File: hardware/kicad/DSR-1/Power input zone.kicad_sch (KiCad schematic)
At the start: 0 parts

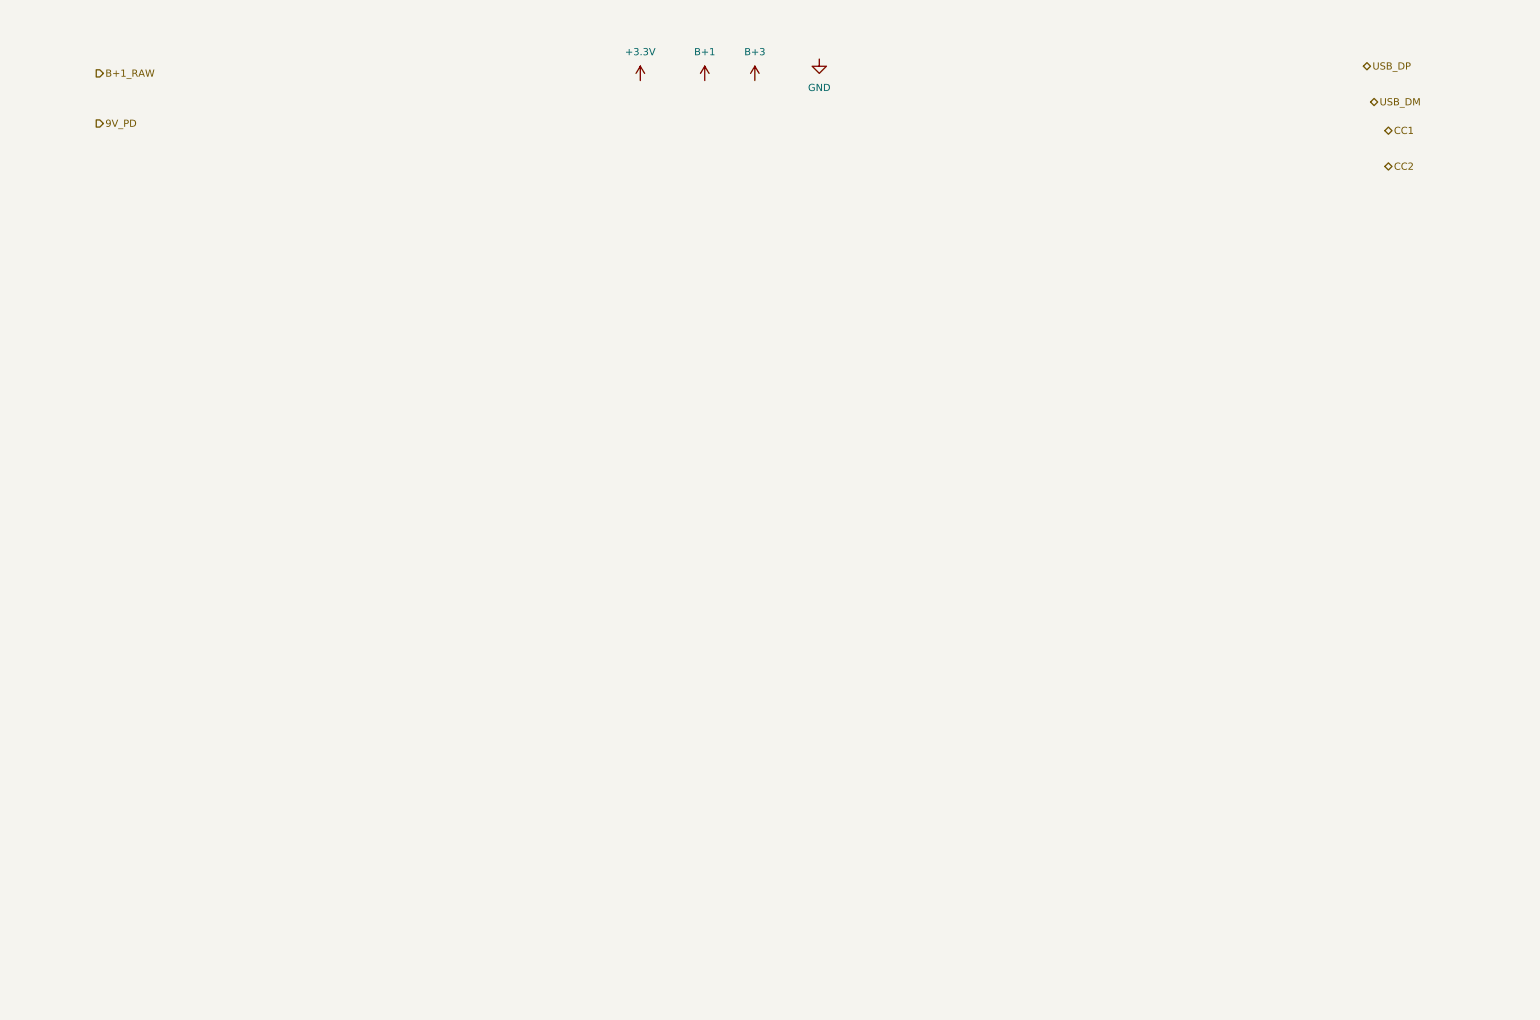
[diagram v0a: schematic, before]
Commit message: updated project symbol library ans started routing power input schematic
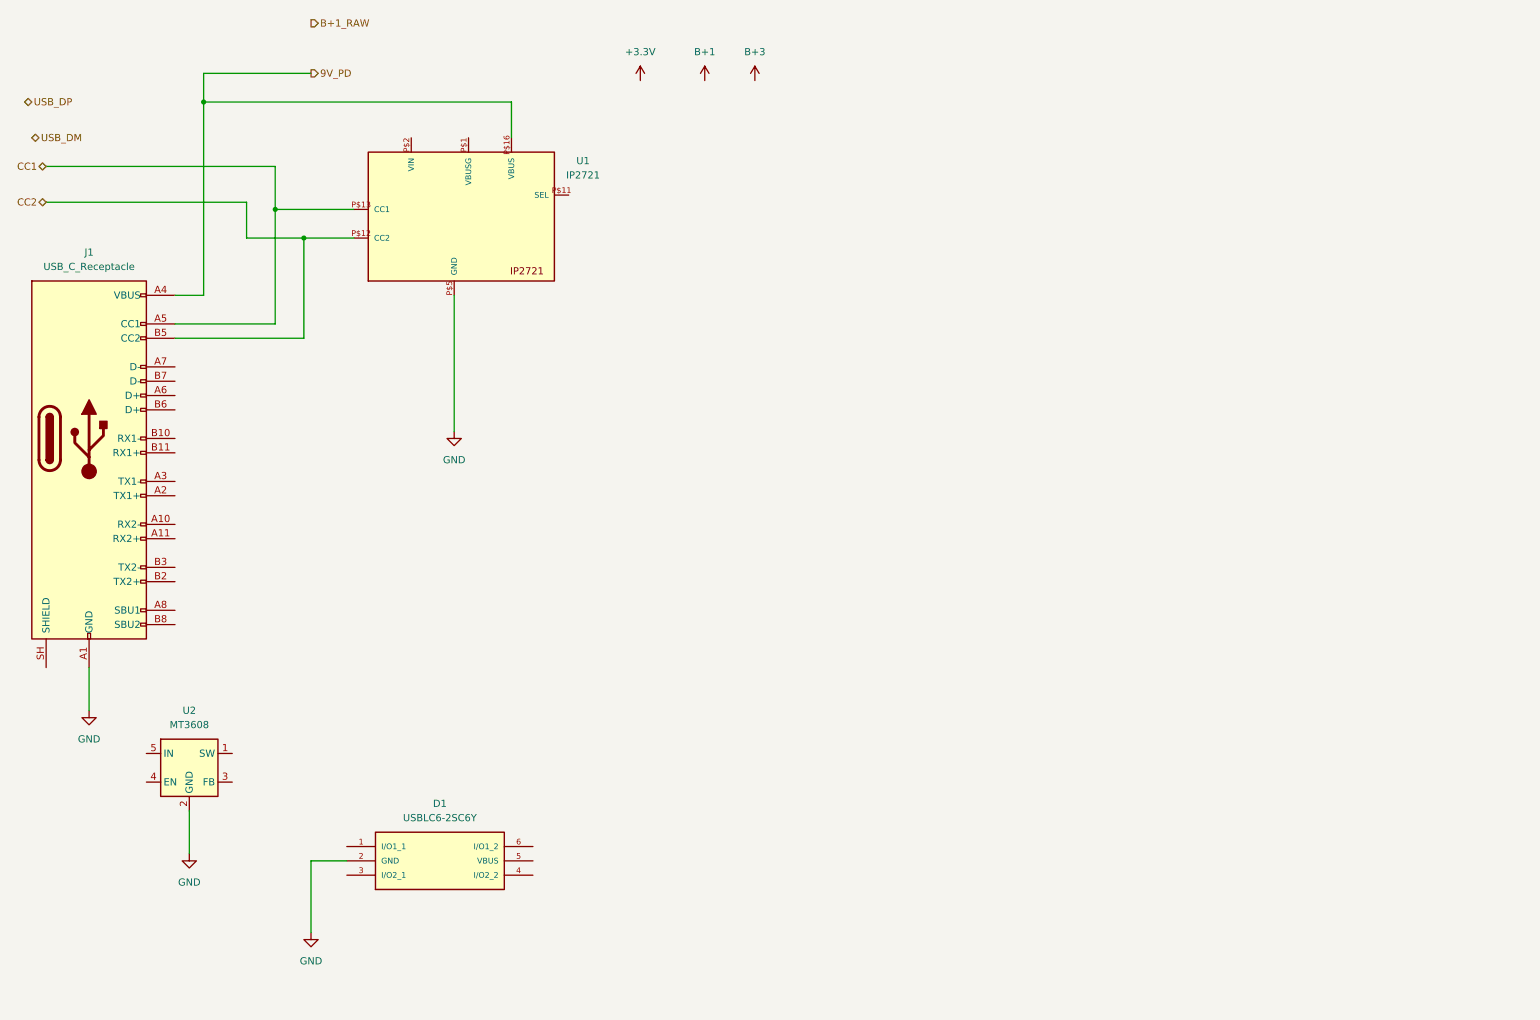
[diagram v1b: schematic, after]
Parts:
- added D1: USBLC6-2SC6Y, USBLC6-2SC6Y:SOT95P280X145-6N, symbol DSR-1:USBLC6-2SC6Y
- added J1: USB_C_Receptacle, symbol DSR-1:USB_C_Receptacle
- added U1: IP2721, IP2721:TSSOP16, symbol DSR-1:IP2721
- added U2: MT3608, Package_TO_SOT_SMD:SOT-23-6, symbol DSR-1:MT3608
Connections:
- net 9V_PD: now also J1.A4 (VBUS), J1.A9 (VBUS), J1.B4 (VBUS), J1.B9 (VBUS), U1.P$16 (VBUS)
- net CC1: now also J1.A5 (CC1), U1.P$13 (CC1)
- net CC2: now also J1.B5 (CC2), U1.P$12 (CC2)
- net GND: now also D1.2 (GND), J1.A1 (GND), J1.A12 (GND), J1.B1 (GND), J1.B12 (GND), U1.P$5 (GND), U2.2 (GND)

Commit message: Completed Power Input Sheet Variant A
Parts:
- removed U2: MT3608, Package_TO_SOT_SMD:SOT-23-6, symbol DSR-1:MT3608
- added C1: 4.7uf, symbol Device:C_US
- added C2: 10uf, symbol Device:C_US
- added C3: 100nf, symbol Device:C_US
- added C4: 22uf, symbol Device:C_US
- added L1: 4.7uH 1.5A, symbol Device:L
- added R1: 649k, symbol Device:R
- added R2: 100k, symbol Device:R
- added U3: AP63203WU-7, AP63203WU-7:SOIC_05WU-7_DIO-M, symbol AP63203WU-7:AP63203WU-7
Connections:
- net +3.3V: now also D1.5 (VBUS)
- net 9V_PD: now also U1.P$11 (SEL), C1.1, C2.1, U3.2 (EN), U3.3 (VIN); no longer J1.A4 (VBUS), J1.A9 (VBUS), J1.B4 (VBUS), J1.B9 (VBUS)
- net B+1: now also C4.1, L1.2, R1.1, R2.1
- net GND: now also J1.SH (SHIELD), C1.2, C2.2, C4.2, R2.2, U3.4 (GND)
- net USB_DM: now also D1.6 (I/O1_2)
- net USB_DP: now also D1.4 (I/O2_2)
- net at D1.1 (I/O1_1): now also J1.A7 (D-), J1.B7 (D-)
- net at D1.3 (I/O2_1): now also J1.A6 (D+), J1.B6 (D+)
- net at U1.P$1 (VBUSG): now also J1.A4 (VBUS), J1.A9 (VBUS), J1.B4 (VBUS), J1.B9 (VBUS), U1.P$2 (VIN)
- new net: C3.1, U3.6 (BST)
- new net: C3.2, L1.1, U3.5 (SW)
- new net: R1.2, U3.1 (FB)
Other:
- note added: "+"
- note added: "10v"
- note added: "16v"
- moved on the sheet: D1, J1, U1

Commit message: Refactor code structure for improved readability and maintainability
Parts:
- added D2, D3, D4, D5: SS14, Diode_SMD:D_SMA, symbol Diode:SS14
- added D6: SMBJ12A-13-F, SMBJ12A-13-F:DIOM5336X250N, symbol SMBJ12A-13-F:SMBJ12A-13-F
- added F1: Polyfuse, symbol Device:Polyfuse
- added J2: Barrel_Jack, symbol Connector:Barrel_Jack
- J1: DNP (none) -> Do Not Populate for Variant B
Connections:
- net GND is gone; now on net B+1: C1.2, C2.2, C4.2, D1.2 (GND), J1.A1 (GND), J1.A12 (GND), J1.B1 (GND), J1.B12 (GND), J1.SH (SHIELD), R2.2, U1.P$5 (GND), U3.4 (GND)
- net B+1: now also D4.2 (A), D5.2 (A), D6.1, D6.2, F1.2
- new net: D2.1 (K), D3.1 (K), F1.1
- new net: D2.2 (A), D4.1 (K), J2.2
- new net: D3.2 (A), D5.1 (K), J2.1
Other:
- note added: "Variant A - USB-C PD/Data"
- note added: "Variant B - Barrel Jack, Polarity Agnostic"
- moved on the sheet: C1, C2, C3, C4, D1, J1, L1, R1, R2, U1, U3

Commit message: Refactor code structure for improved readability and maintainability
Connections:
- net B+1: no longer C1.2, C2.2, C4.2, D1.2 (GND), D4.2 (A), D5.2 (A), D6.1, D6.2, F1.2, J1.A1 (GND), J1.A12 (GND), J1.B1 (GND), J1.B12 (GND), J1.SH (SHIELD), R2.2, U1.P$5 (GND), U3.4 (GND)
- net 9V_PD renamed GND
- net GND: now also C1.2, C2.2, C4.2, D1.2 (GND), D4.2 (A), D5.2 (A), D6.1, D6.2, F1.2, J1.A1 (GND), J1.A12 (GND), J1.B1 (GND), J1.B12 (GND), J1.SH (SHIELD), R2.2, U1.P$5 (GND), U3.4 (GND)
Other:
- note added: "B+1 output = 0.8 × (1 + 649k/100k) = 6.19V EN tied to VIN - AP63203 internal clamp handles 9V input safely. C3 (BST cap) must be placed within 1mm of BST/SW pins on PCB."
- note added: "BRING-UP ORDER: 1. Verify 9V_PD present before AP63203 powers up 2. Check B+1 = 6.0-6.2V before enabling downstream 3. Check B+3 = 10.5-11V (no load) 4. Check +3.3V = 3.3V ±2% 5. Do not connect WM-D6C harness until all rails verified"
- note added: "SEL pin sets PD voltage request - verify correct resistor value against IP2721 datasheet for 9V profile before ordering PCB. VBUSG must be tied to VIN. Floating VBUSG prevents output enable after negotiation regardless of CC state."
- note added: "Variant B input: 9V DC nominal, 5.5mm/2.1mm barrel jack. Polarity agnostic - bridge rectifier output is always positive. Do NOT connect a 6V adapter - minimum 7.5V required after 0.8V bridge drop to maintain regulation headroom. SMBJ12A: standoff 12V, clamp 19.9V max. AP63203 VIN abs max 32V."
- moved on the sheet: C2, C3, C4, D2, D3, D4, D5, D6, F1, J2, L1, R1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

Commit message: Completed microcontroller schematic
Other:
- title: (none) -> Power Input Zone
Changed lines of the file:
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@@
 	(generator_version "10.0")
 	(paper "A4")
+	(title_block
+		(title "Power Input Zone")
+		(date "2026-05-31")
+		(rev "1")
+	)
 	(text "BRING-UP ORDER:\n1. Verify 9V_PD present before AP63203 powers up\n2. Check B+1 = 6.0-6.2V before enabling downstream\n3. Check B+3 = 10.5-11V (no load)\n4. Check +3.3V = 3.3V ±2%\n5. Do not connect WM-D6C harness until all rails verified"
 		(exclude_from_sim no)
